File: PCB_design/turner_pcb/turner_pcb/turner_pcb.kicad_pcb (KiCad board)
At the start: 2 copper layers, 79.1 x 90 mm, 6 parts, among them P1 Digital, P2 Analog, P3 CONN_01X01, P4 CONN_01X01, P5 CONN_01X01, P6 CONN_01X01

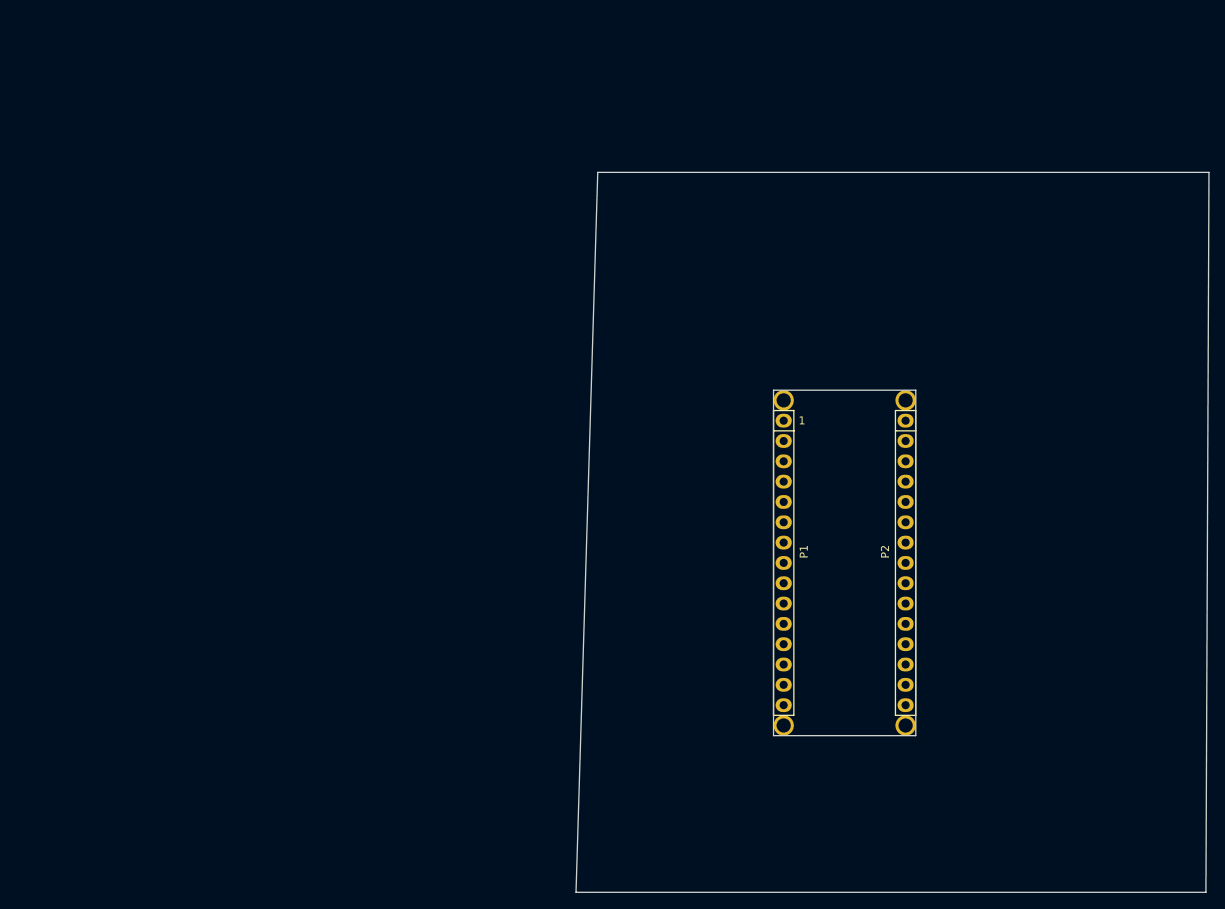
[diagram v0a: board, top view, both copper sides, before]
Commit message: first attempt at including tmc2208
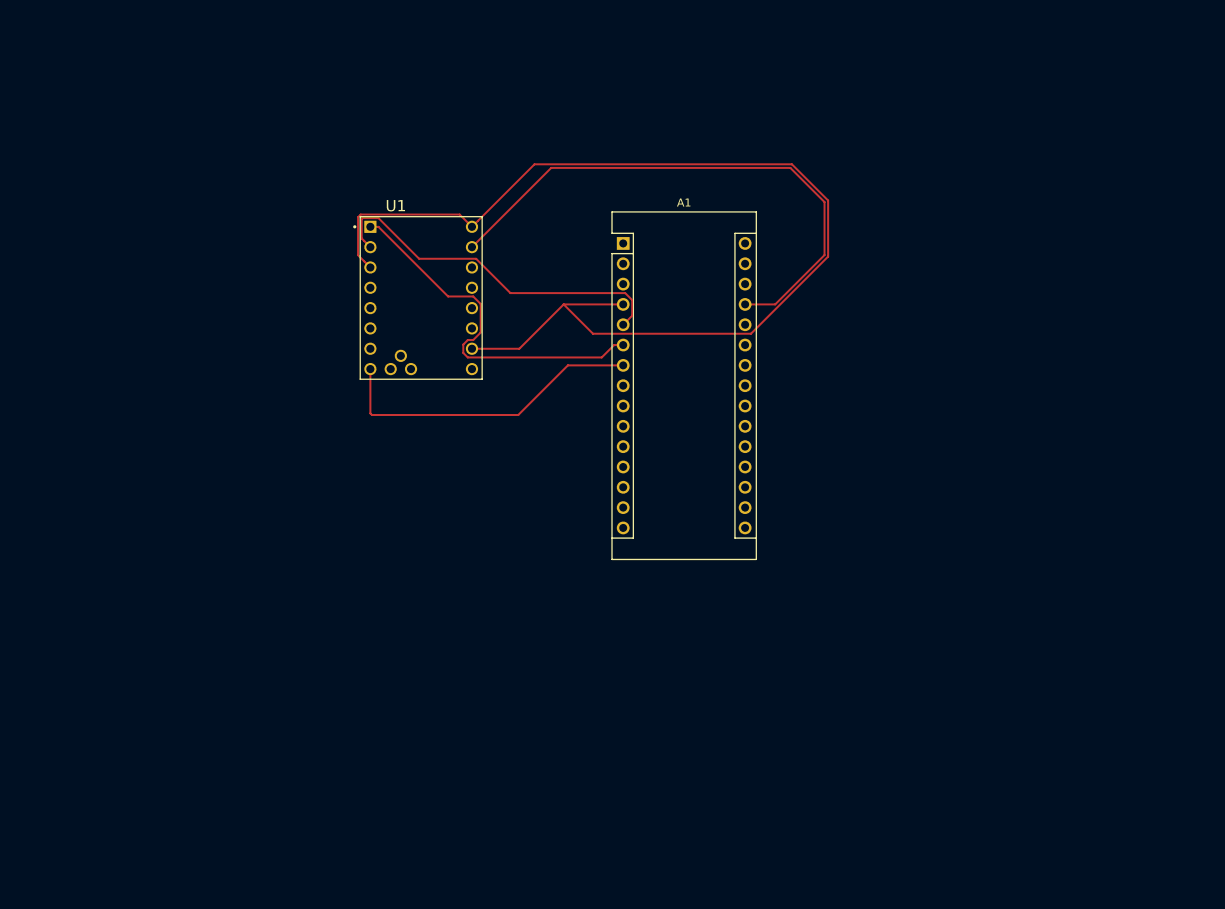
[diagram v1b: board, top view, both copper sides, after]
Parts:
- removed P1: Digital, Socket_Arduino_Nano:Socket_Strip_Arduino_1x15
- removed P2: Analog, Socket_Arduino_Nano:Socket_Strip_Arduino_1x15
- removed P3, P4, P5, P6: CONN_01X01, Socket_Arduino_Nano:1pin_Nano
- added A1: Arduino_Nano_v3.x, Module:Arduino_Nano, F.Cu at (119.4, 49.1)
- added U1: TMC2208_SILENTSTEPSTICK, TMC2208_SILENTSTEPSTICK:MODULE_TMC2208_SILENTSTEPSTICK, F.Cu at (94.1, 55.9)
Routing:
- net GND: track 0.00 -> 138.3 mm
- net +5V: track 0.00 -> 69.0 mm
- net Direction: track 0.00 -> 46.1 mm
- net Step: track 0.00 -> 45.6 mm
- net Enable: track 0.00 -> 39.8 mm
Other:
- board outline removed
- board text removed: "1"

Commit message: first complete version on pcb
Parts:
- removed U1: TMC2208_SILENTSTEPSTICK, TMC2208_SILENTSTEPSTICK:MODULE_TMC2208_SILENTSTEPSTICK
- added 12V: Conn_01x02, Connector_Molex:Molex_Micro-Fit_3.0_43045-0212_2x01_P3.00mm_Vertical, F.Cu at (55.7, 42.9)
- added C1: C_Small, Capacitor_SMD:C_0603_1608Metric, F.Cu at (63.9, 70.2)
- added C2: C_Polarized, Capacitor_THT:CP_Radial_D8.0mm_P5.00mm, F.Cu at (52.2, 32.0)
- added Driver: TMC2208_SILENTSTEPSTICK, TMC2208_SILENTSTEPSTICK:MODULE_TMC2208_SILENTSTEPSTICK, F.Cu at (74.1, 62.8)
- added General IO: Conn_02x03_Odd_Even, Connector_Molex:Molex_Micro-Fit_3.0_43045-0612_2x03_P3.00mm_Vertical, F.Cu at (76.8, 33.6)
- added Pot: Conn_02x02_Odd_Even, Connector_Molex:Molex_Micro-Fit_3.0_43045-0412_2x02_P3.00mm_Vertical, F.Cu at (55.7, 53.1)
- added Stepper: Conn_02x02_Odd_Even, Connector_Molex:Molex_Micro-Fit_3.0_43045-0412_2x02_P3.00mm_Vertical, F.Cu at (55.7, 66.3)
- moved Processor 25.1 mm to (104.2, 69.1), turned to 180 degrees
- renumbered A1 to Processor
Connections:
- Processor pad 10: Net-(A1-Pad10) -> DIO3
- Processor pad 11: Net-(A1-Pad11) -> DIO4
- Processor pad 19: Net-(A1-Pad19) -> Pot
- Processor pad 20: Net-(A1-Pad20) -> AO1
- Processor pad 30: Net-(A1-Pad30) -> +12V
- Processor pad 8: Net-(A1-Pad8) -> DIO1
- Processor pad 9: Net-(A1-Pad9) -> DIO2
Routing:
- net GND: track 138.3 -> 4.36 mm
- net +12V: track 0.00 -> 100.6 mm
- net DIO2: track 0.00 -> 62.2 mm
- net Pot: track 0.00 -> 52.7 mm
- net DIO4: track 0.00 -> 43.7 mm
- net DIO1: track 0.00 -> 42.7 mm
- net DIO3: track 0.00 -> 42.3 mm
- net AO1: track 0.00 -> 24.8 mm
- net DA2: track 0.00 -> 18.1 mm
- net DB2: track 0.00 -> 17.1 mm
- net +5V: track 69.0 -> 53.6 mm
- net Enable: track 39.8 -> 24.7 mm
- net DB1: track 0.00 -> 14.3 mm
- net DA1: track 0.00 -> 14.1 mm
- net Step: track 45.6 -> 36.8 mm
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- added copper zone on B.Cu, net GND
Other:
- board outline added: 66 x 57.1 mm
- board text added: "+"
- board text added: "-"

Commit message: worked on pcb design
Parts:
- removed Driver: TMC2208_SILENTSTEPSTICK, TMC2208_SILENTSTEPSTICK:MODULE_TMC2208_SILENTSTEPSTICK
- added A2: Pololu_Breakout_A4988, Module:Pololu_Breakout-16_15.2x20.3mm, F.Cu at (103.1, 59.3)
- General_IO1: renamed from General IO
- moved stepper1 54.5 mm to (98.2, 32.2), turned to 180 degrees
- moved C1 44.6 mm to (106.8, 57.9)
- moved General_IO1 38.7 mm to (93.6, 68.5), turned to 0 degrees
- moved A1 25.5 mm to (78.9, 66.5)
- moved pot_input1 6.06 mm to (55.0, 59.1)
- moved input_power1 3.37 mm to (55.2, 46.2)
- moved C2 3.34 mm to (51.0, 35.1)
- renumbered Processor to A1, 12V to input_power1, Pot to pot_input1, Stepper to stepper1
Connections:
- A1 pad 12: Net-(A1-Pad12) -> MS1
- A1 pad 13: Net-(A1-Pad13) -> MS2
- A1 pad 14: Net-(A1-Pad14) -> MS3
- A1 pad 20: AO1 -> Net-(A1-Pad20)
- General_IO1 pad 2: AO1 -> +5V
- stepper1 pad 1: DA1 -> M1A
- stepper1 pad 2: DB1 -> M1B
- stepper1 pad 3: DA2 -> M2A
- stepper1 pad 4: DB2 -> M2B
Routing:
- net +12V: track 100.6 -> 0.00 mm
- net DIO1: track 42.7 -> 71.3 mm
- net +5V: track 53.6 -> 81.9 mm
- net Direction: track 44.7 -> 17.2 mm
- net MS2: track 0.00 -> 25.9 mm
- net DIO2: track 62.2 -> 36.9 mm
- net M1B: track 0.00 -> 25.2 mm
- net Step: track 36.8 -> 11.7 mm
- net M2B: track 0.00 -> 24.9 mm
- net AO1: track 24.8 -> 0.00 mm
- net Pot: track 52.7 -> 29.3 mm
- net M2A: track 0.00 -> 22.6 mm
- net M1A: track 0.00 -> 22.1 mm
- net MS3: track 0.00 -> 20.4 mm
- net DA2: track 18.1 -> 0.00 mm
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- added copper zone on F.Cu, net +12V

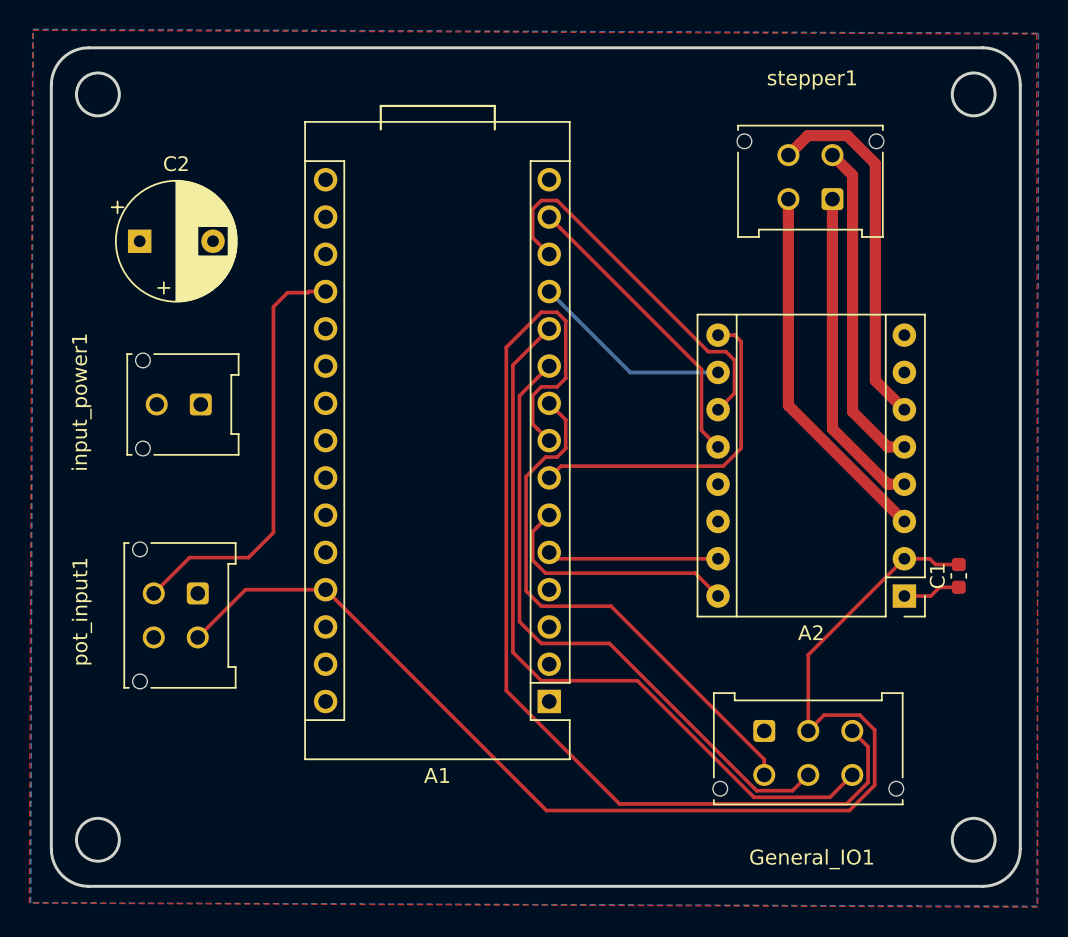
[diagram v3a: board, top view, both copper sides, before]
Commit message: pcb design V1.0 sent to JLCPCB
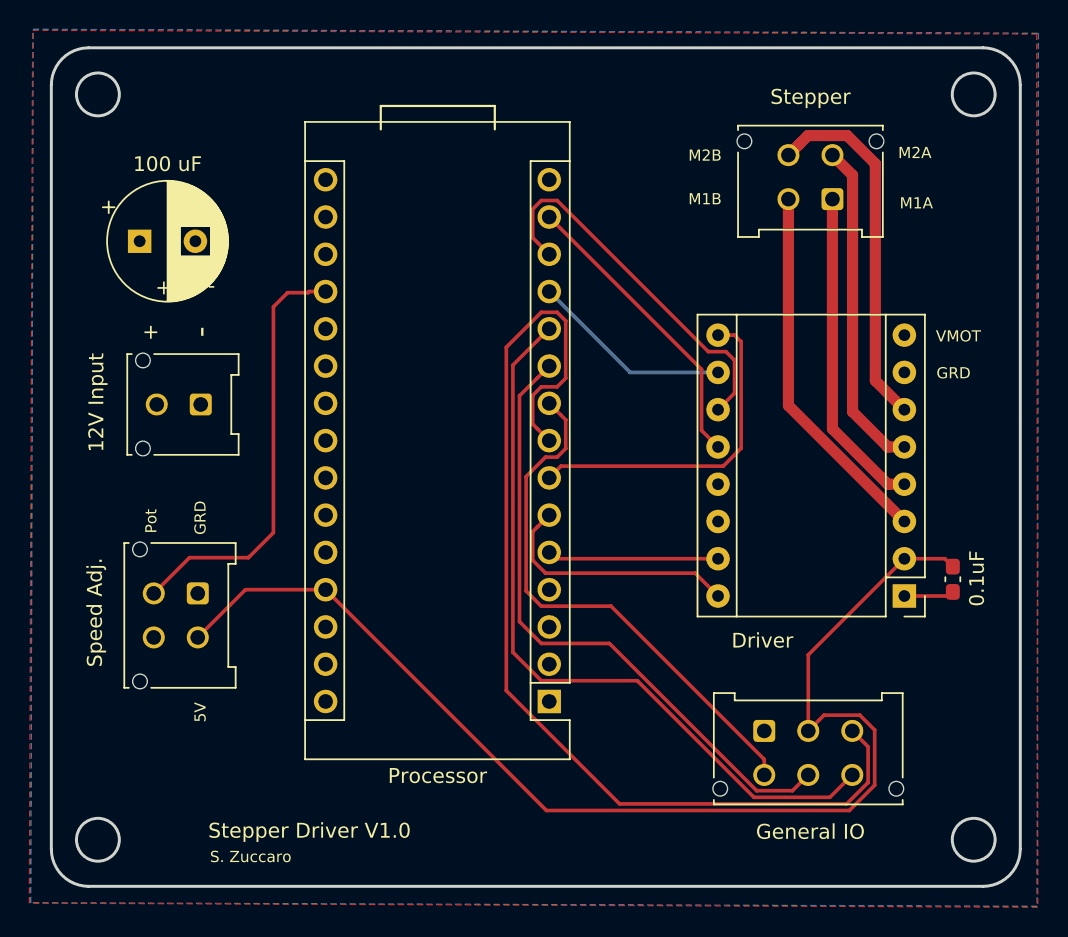
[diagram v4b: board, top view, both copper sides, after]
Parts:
- removed C1: C_Small, Capacitor_SMD:C_0603_1608Metric
- added 0.1uF: C, Capacitor_SMD:C_0603_1608Metric_Pad1.08x0.95mm_HandSolder, F.Cu at (106.4, 58.1)
- 100 uF: renamed from C2; footprint Capacitor_THT:CP_Radial_D8.0mm_P5.00mm -> Capacitor_THT:CP_Radial_D8.0mm_P3.80mm
- 12V Input: renamed from input_power1
- General IO: renamed from General_IO1
- Speed Adj.: renamed from pot_input1
- renumbered A2 to Driver, A1 to Processor, stepper1 to Stepper
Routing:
- net GND: track 3.96 -> 3.42 mm
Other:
- board text added: "5V"
- board text added: "GRD"
- board text added: "M1A"
- board text added: "M1B"
- board text added: "M2A"
- board text added: "M2B"
- board text added: "Pot"
- board text added: "S. Zuccaro"
- board text added: "Stepper Driver V1.0"
- board text added: "VMOT"
